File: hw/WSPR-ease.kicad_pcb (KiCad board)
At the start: 4 copper layers, 99 x 64 mm, 169 parts, among them IC401 SN74AHCT1G125DRLR, IC402 SN74AHCT1G125DRLR, IC403 SN74AHCT1G125DRLR, IC501 SN74AHCT1G125DRLR, IC502 SN74AHCT1G125DRLR, IC503 SN74AHCT1G125DRLR, IC601 SN74AHCT1G125DRLR, IC602 SN74AHCT1G125DRLR, IC603 SN74AHCT1G125DRLR, IC701 SN74AHCT1G125DRLR, IC702 SN74AHCT1G125DRLR, IC703 SN74AHCT1G125DRLR, J101 SMA, J102 pwr+data, J103 SMA, K201 G6K-2, K202 G6K-2, K203 G6K-2, Q101 2N7002H, Q201 2N7002H, Q202 2N7002H, Q203 2N7002H, Q401 MMBF170, Q402 MMBF170, Q403 MMBF170, Q501 MMBF170, Q502 MMBF170, Q503 MMBF170, Q601 MMBF170, Q602 MMBF170, Q603 MMBF170, Q701 MMBF170, Q702 MMBF170, Q703 MMBF170, T301 BN-43-202_DualPri_CTSec, U101 GNSS module, U102 ESP32-S3-WROOM-1-N8R8, U103 SRV05-4, U104 TPS74612PQWDRBRQ1, U105 TPS22918DBVR, U106 LMR51430YDDCR, U301 ICE40UP5K-SG48ITR, Y301 40MHz

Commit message: Timing now closes at 121MHz. But output still does not produce any signal on my scope. Shit.
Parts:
- removed C201, C211: 100nF X7R 50V, Capacitor_SMD:C_0603_1608Metric
- moved L205 0.06 mm to (115.6, 94.5)
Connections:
- K201 pad 4: Net-(C201-Pad2) -> /Low Pass Filters/RFin
- K201 pad 5: Net-(C211-Pad1) -> /Low Pass Filters/RFout
- K202 pad 4: Net-(C201-Pad2) -> /Low Pass Filters/RFin
- K202 pad 5: Net-(C211-Pad1) -> /Low Pass Filters/RFout
- K203 pad 4: Net-(C201-Pad2) -> /Low Pass Filters/RFin
- K203 pad 5: Net-(C211-Pad1) -> /Low Pass Filters/RFout
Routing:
- net /Low Pass Filters/RFout: track 7.32 -> 88.2 mm, vias 0 -> 4
- net Net-(C211-Pad1): track 79.6 -> 0.00 mm, vias 4 -> 0
- net /Low Pass Filters/RFin: track 17.3 -> 90.0 mm, vias 0 -> 4
- net Net-(C201-Pad2): track 71.7 -> 0.00 mm, vias 4 -> 0

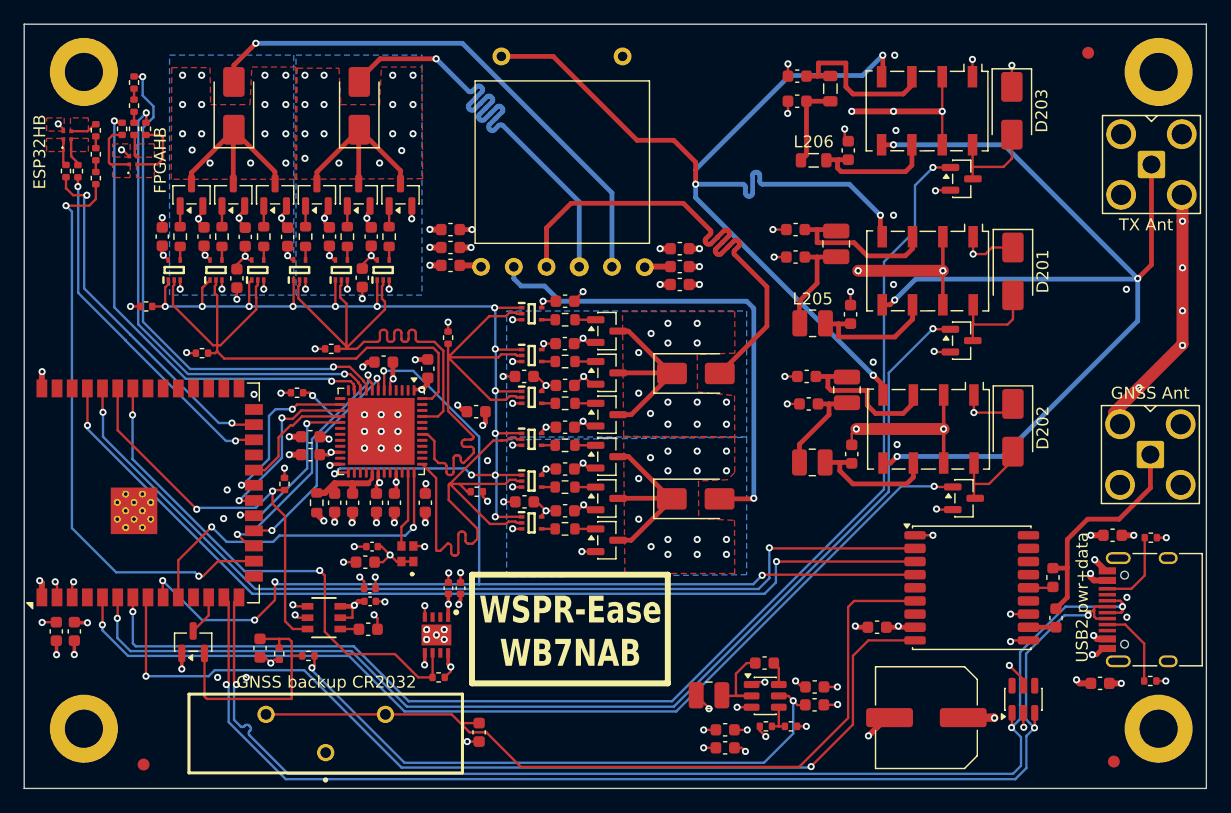
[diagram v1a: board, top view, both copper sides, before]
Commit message: Use VFPGAIO for pullup for driverNEN. Fix some layout issues with more equal routing lengths in critical tx phase paths.
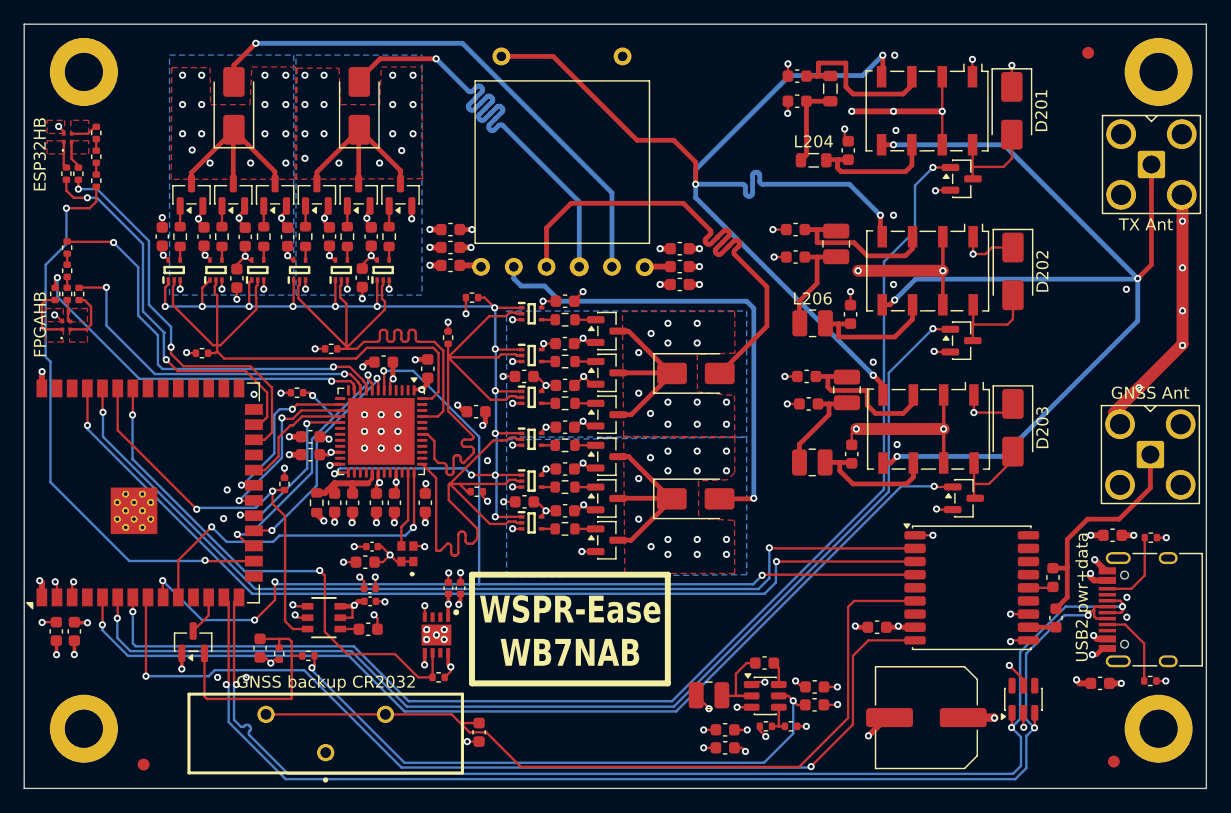
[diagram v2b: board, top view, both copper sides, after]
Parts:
- moved R306 27.3 mm to (87.1, 92.3)
- moved R301 14.9 mm to (53.2, 88.1)
- moved R302 14.9 mm to (53.2, 90.0)
- moved D301 14.9 mm to (53.1, 94.6)
- moved R303 14.9 mm to (54.2, 92.0)
- moved R304 14.9 mm to (52.2, 92.0)
- moved R305 14.9 mm to (53.2, 92.0)
- moved D101 0.22 mm to (53.2, 78.9)
- moved R107 0.22 mm to (54.1, 81.9)
- moved R103 0.22 mm to (55.6, 82.5)
- moved R106 0.22 mm to (55.6, 80.5)
- moved R108 0.22 mm to (53.1, 81.9)
- moved R109 0.22 mm to (55.6, 78.5)
- renumbered C204 to C201, C207 to C204, C210 to C207, C402 to C401, C401 to C402, C502 to C501, C501 to C502, C602 to C601, C601 to C602, C702 to C701, C701 to C702, D203 to D201, D201 to D202, D202 to D203, IC402 to IC401, IC401 to IC402, IC502 to IC501, IC501 to IC502, IC602 to IC601, IC601 to IC602, IC702 to IC701, IC701 to IC702, K203 to K201, K201 to K202, K202 to K203, L203 to L201, L201 to L202, L202 to L203, L206 to L204, L204 to L205, L205 to L206, Q203 to Q201, Q201 to Q203, R107 to R103, R108 to R104, R109 to R105, R110 to R106, R111 to R107, R112 to R108, R113 to R109, R114 to R110, R115 to R111, R116 to R112, R117 to R113
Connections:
- R306 pad 2: +3.3V -> +VFPGAIO
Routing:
- net /Transmitter/hbG: track 40.0 -> 29.3 mm
- net /Transmitter/hbR: track 43.5 -> 34.5 mm
- net /Transmitter/hbB: track 39.6 -> 30.9 mm
- net Net-(U102-IO47): track 29.6 -> 33.9 mm
- net Net-(U102-IO48): track 29.8 -> 32.3 mm
- net +VFPGAIO: track 18.3 -> 19.6 mm, vias 9 -> 10
- net /Transmitter/grn: track 5.65 -> 4.64 mm
- net Net-(U102-IO46): track 48.6 -> 47.6 mm
- net +3.3V: track 24.6 -> 23.8 mm, vias 18 -> 17
- net /Transmitter/driverNEN: track 88.1 -> 88.8 mm

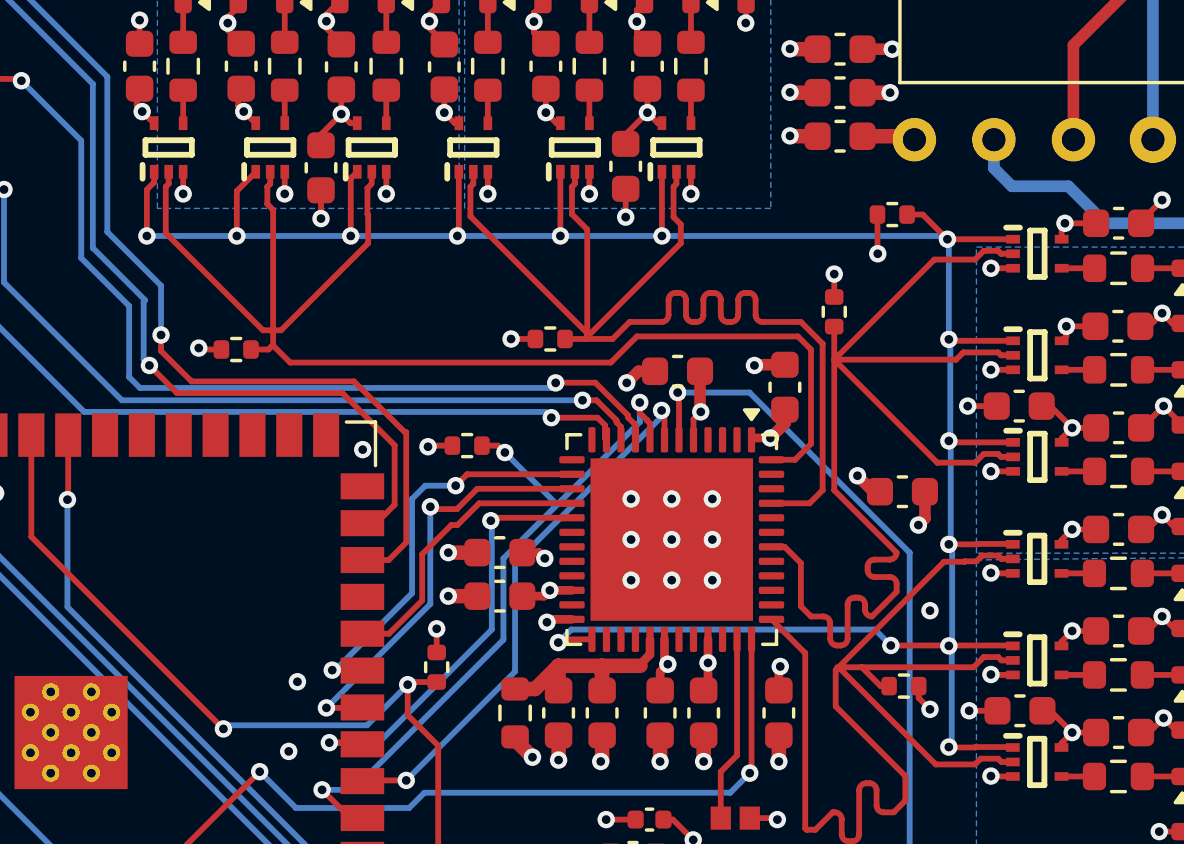
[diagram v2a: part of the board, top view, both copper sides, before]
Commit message: I think this is now using the SB_MAC16 properly for each instance. The AI based configs were all screwed up. I listed teh name from the iCE40 Tech Lib doc for each flavor used in a comment to help if changes are needed later. Also silkscreen labels for the four FPGA output pins for probing. I also fixed some stuff in the SB_IO sim cells_sim.v that seemed wrong but now it matches the PDF block diagram AFACT.
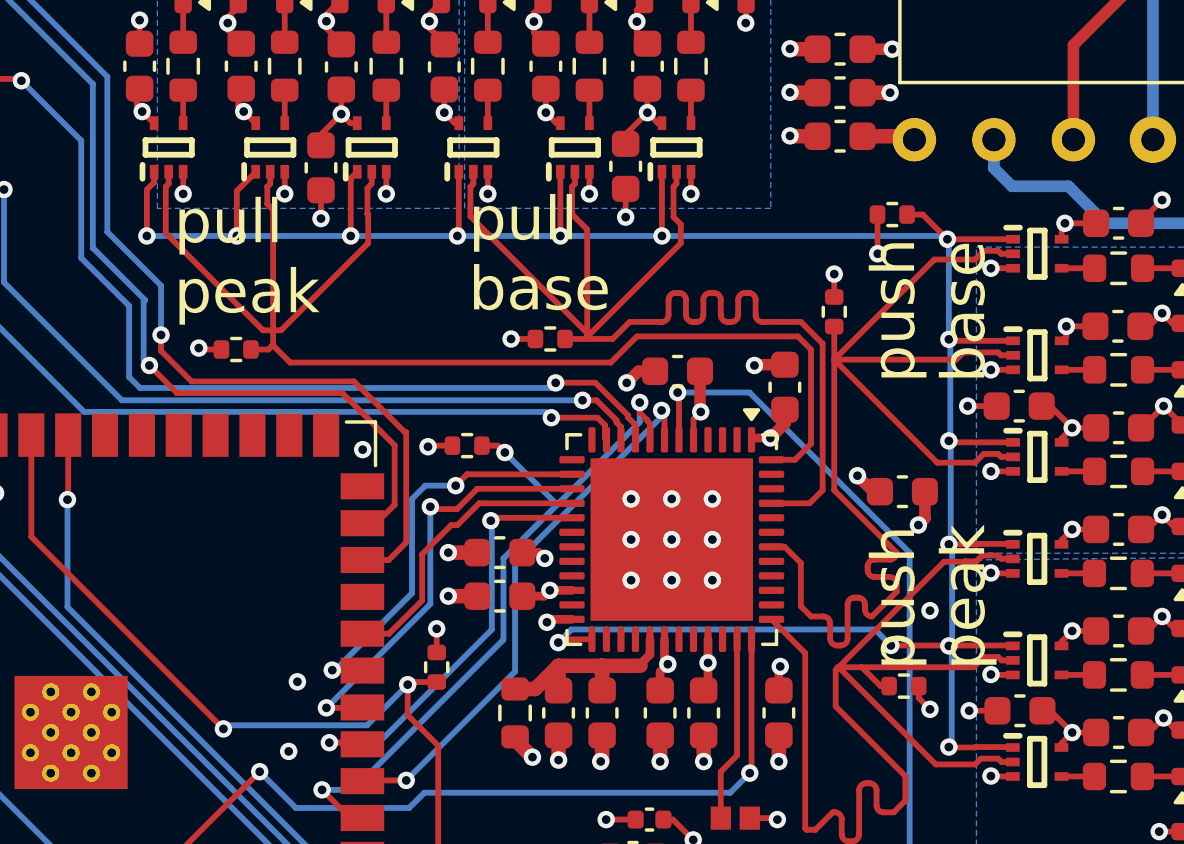
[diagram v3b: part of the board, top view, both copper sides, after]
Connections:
- net /Transmitter/pull1 renamed /Transmitter/pullBase
- net /Transmitter/pull1D renamed /Transmitter/pullBaseD
- net /Transmitter/pull1T renamed /Transmitter/pullBaseT
- net /Transmitter/pull2 renamed /Transmitter/pullPeak
- net /Transmitter/pull2D renamed /Transmitter/pullPeakD
- net /Transmitter/pull2T renamed /Transmitter/pullPeakT
- net /Transmitter/push1 renamed /Transmitter/pushBase
- net /Transmitter/push1D renamed /Transmitter/pushBaseD
- net /Transmitter/push1T renamed /Transmitter/pushBaseT
- net /Transmitter/push2 renamed /Transmitter/pushPeak
- net /Transmitter/push2D renamed /Transmitter/pushPeakD
- net /Transmitter/push2T renamed /Transmitter/pushPeakT
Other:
- board text added: "pull base"
- board text added: "pull peak"
- board text added: "push base"
- board text added: "push peak"

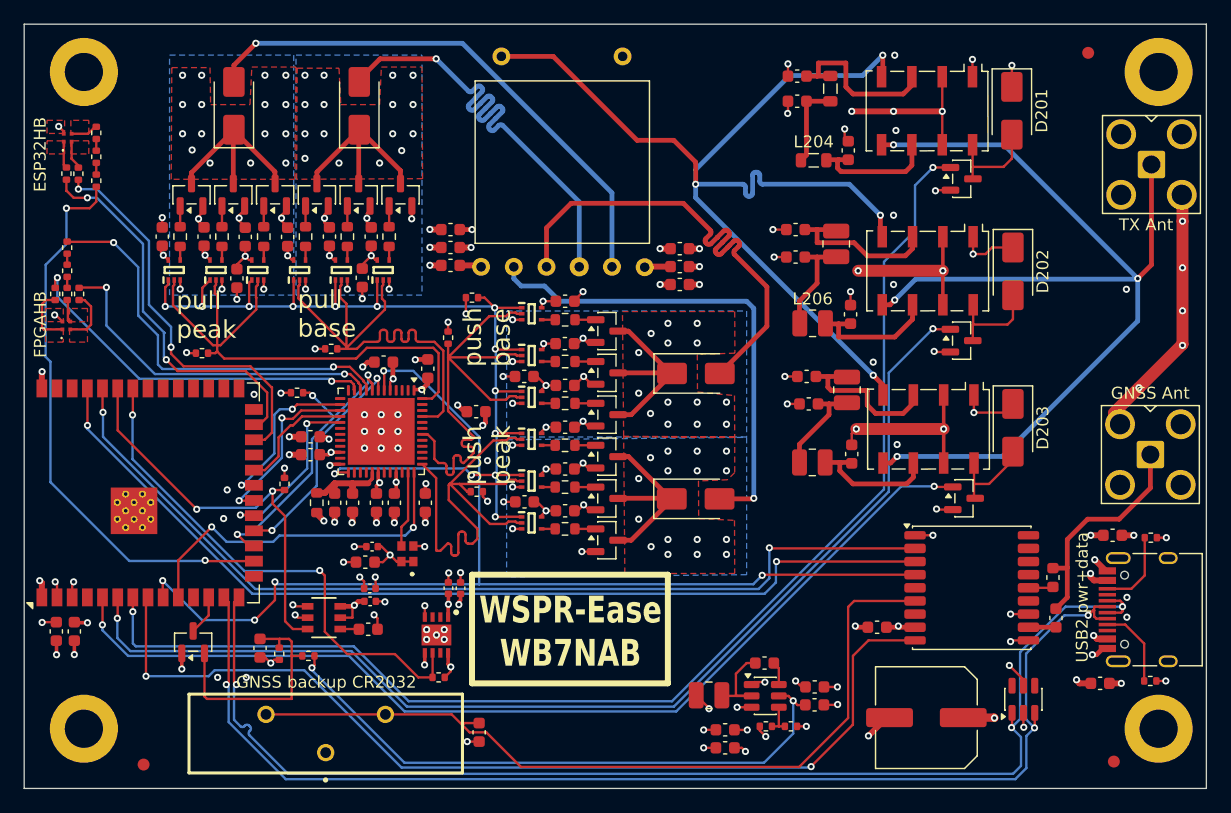
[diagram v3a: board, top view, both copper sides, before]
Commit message: Fucking USB 16-pin footprint! Also, completely redid the layout and wiring of the transmitter using a MOSFET gate and R+diode gate drive, simplify BOM, enhance LPFs for square wave output >= 10MHz.
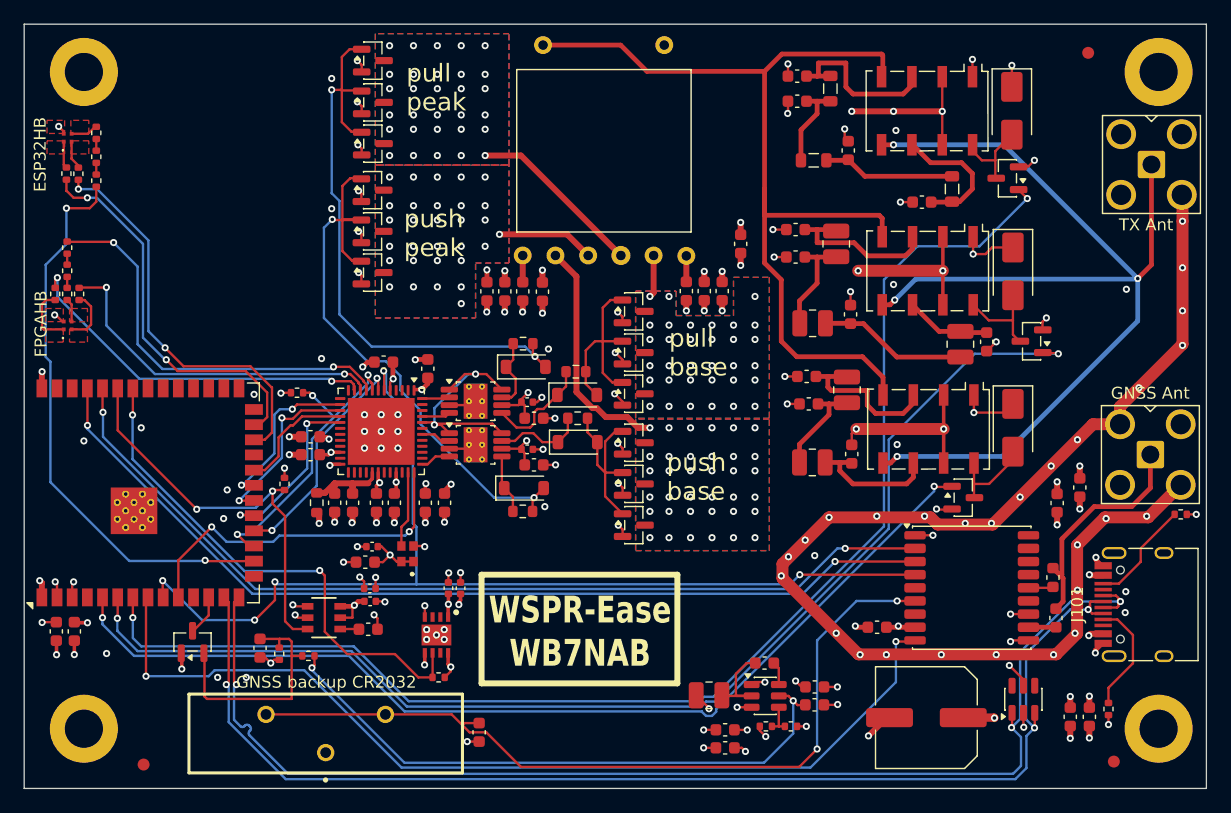
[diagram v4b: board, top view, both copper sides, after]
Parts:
- removed C403, C503, C601, C602, C603, C701, C702, C703: 100nF X7R 50V, Capacitor_SMD:C_0603_1608Metric
- removed D601, D701: SS14, Diode_SMD:D_SMA
- removed IC401, IC402, IC403, IC501, IC502, IC503, IC601, IC602, IC603, IC701, IC702, IC703: SN74AHCT1G125DRLR, Library:SOTFL50P160X60-5N
- removed Q601, Q602, Q603, Q701, Q702, Q703: MMBF170, Package_TO_SOT_SMD:SOT-23
- removed the R306 at (87.1, 92.3)
- removed R308, R309, R310, R311: 10k, Resistor_SMD:R_0402_1005Metric
- removed R403, R503, R601, R602, R603, R701, R702, R703: 10, Resistor_SMD:R_0603_1608Metric
- added C207: 150pF NP0 100V, Capacitor_SMD:C_0603_1608Metric, F.Cu at (130.2, 96.0)
- added C211: 82pF NP0 100V, Capacitor_SMD:C_0603_1608Metric, F.Cu at (124.8, 84.3)
- added D402: 1N4148W, Diode_SMD:D_SOD-123, F.Cu at (91.5, 108.2)
- added D502: 1N4148W, Diode_SMD:D_SOD-123, F.Cu at (95.9, 100.5)
- added L205: 560nH, Inductor_SMD:L_1008_2520Metric, F.Cu at (128.0, 96.2)
- added L208: 270nH, Inductor_SMD:L_0805_2012Metric, F.Cu at (127.3, 83.2)
- added Q404: MMBF170, Package_TO_SOT_SMD:SOT-23, F.Cu at (78.8, 83.3)
- added Q405: MMBF170, Package_TO_SOT_SMD:SOT-23, F.Cu at (78.8, 86.8)
- added Q406: MMBF170, Package_TO_SOT_SMD:SOT-23, F.Cu at (78.8, 90.2)
- added Q504: MMBF170, Package_TO_SOT_SMD:SOT-23, F.Cu at (100.6, 93.5)
- added Q505: MMBF170, Package_TO_SOT_SMD:SOT-23, F.Cu at (100.6, 96.9)
- added Q506: MMBF170, Package_TO_SOT_SMD:SOT-23, F.Cu at (100.6, 100.3)
- added U401: UCC27524DGN, Package_SO:Texas_DGN0008G_VSSOP-8-1EP_3x3mm_P0.65mm_EP2x2.94mm_Mask1.846x2.15mm_ThermalVias, F.Cu at (87.4, 104.6)
- added U501: UCC27524DGN, Package_SO:Texas_DGN0008G_VSSOP-8-1EP_3x3mm_P0.65mm_EP2x2.94mm_Mask1.846x2.15mm_ThermalVias, F.Cu at (87.4, 101.0)
- C204: renamed from C203; value 220pF NP0 100V -> 150pF NP0 100V
- C205: renamed from C206; value 470pF NP0 100V -> 330pF NP0 100V
- C206: renamed from C209; value 220pF NP0 100V -> 330pF NP0 100V
- C208: renamed from C201; value 100pF NP0 100V -> 82pF NP0 100V
- C209: renamed from C204; value 220pF NP0 100V -> 180pF NP0 100V
- C210: renamed from C207; value 100pF NP0 100V -> 180pF NP0 100V
- C401, C501: value 100nF X7R 50V -> 1uF; footprint Capacitor_SMD:C_0603_1608Metric -> Capacitor_SMD:C_0402_1005Metric
- D401, D501: value SS14 -> 1N4148W; footprint Diode_SMD:D_SMA -> Diode_SMD:D_SOD-123
- L204: renamed from L206; value 560nH -> 680nH
- L207: renamed from L204; value 270nH -> 330nH
- Q101, Q201, Q202, Q203: value 2N7002H -> MMBF170
- moved C307 49.1 mm to (137.2, 127.4), turned to 90 degrees
- moved C306 47.4 mm to (138.0, 108.2), turned to -90 degrees
- moved Q503 38.6 mm to (78.8, 79.4)
- moved Q501 38.5 mm to (78.8, 72.5)
- moved Q502 38.5 mm to (78.8, 76.0)
- moved C305 31.8 mm to (109.6, 87.8), turned to -90 degrees
- moved Q203 27.0 mm to (131.9, 82.3), turned to 180 degrees
- moved Q201 26.7 mm to (128.2, 109.0)
- moved C301 25.6 mm to (93.0, 91.8)
- moved D501 18.0 mm to (91.6, 98.1)
- moved R402 13.0 mm to (91.3, 110.2)
- moved C401 12.8 mm to (91.7, 105.0)
- moved D401 11.4 mm to (96.0, 104.4)
- moved C402 10.5 mm to (92.3, 106.3)
- moved R502 9.71 mm to (95.8, 98.5)
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- renumbered C110 to C101, C111 to C102, C105 to C103, C112 to C104, C106 to C105, C101 to C106, C103 to C107, C104 to C108, C102 to C109, C115 to C110, C113 to C111, C114 to C112, C116 to C113, C117 to C114, C108 to C115, C109 to C116, C107 to C117, C202 to C201, C205 to C202, C208 to C203, C309 to C301, C316 to C302, C318 to C303, C321 to C304, C307 to C305, C310 to C306, C308 to C307, C301 to C308, C302 to C309, C313 to C310, C317 to C311, C319 to C312, C320 to C313, C324 to C314, C314 to C315, C311 to C316, C315 to C317, C312 to C318, C322 to C319, C303 to C320, C305 to C321, C323 to C322, C304 to C323, C306 to C324, D203 to D201, D201 to D203, J102 to J101, J103 to J102, J101 to J103, K202 to K201, K203 to K202, K201 to K203, L202 to L201, L205 to L202, L201 to L206, R110 to R101, R111 to R102, R101 to R103, R102 to R104, R103 to R105, R109 to R107, R107 to R108, R108 to R109, R104 to R110, R112 to R111, R113 to R112, R105 to R113, R305 to R303, R303 to R304, R304 to R305, R307 to R306, R312 to R307, U103 to U101, U106 to U103, U101 to U104, U104 to U105, U105 to U106
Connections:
- C206 pad 1: Net-(C209-Pad1) (its old number) -> Net-(C206-Pad1)
- C210 pad 1: Net-(C207-Pad1) -> Net-(C210-Pad1)
- D201 pad 2: Net-(D203-A) -> Net-(D201-A)
- D203 pad 2: Net-(D201-A) -> Net-(D203-A)
- D401 pad 1: /Transmitter/pushBaseD -> Net-(D401-K)
- D401 pad 2: /Transmitter/pushBaseT -> Net-(D401-A)
- D501 pad 1: /Transmitter/pushPeakD -> Net-(D501-K)
- D501 pad 2: /Transmitter/pushPeakT -> Net-(D501-A)
- K201 pad 8: Net-(D203-A) -> Net-(D201-A)
- K202 pad 6: Net-(C209-Pad1) (its old number) -> Net-(C207-Pad1)
- K203 pad 6: Net-(C207-Pad1) -> Net-(C211-Pad1)
- K203 pad 8: Net-(D201-A) -> Net-(D203-A)
- L204 pad 2: Net-(C209-Pad1) (its old number) -> Net-(C206-Pad1)
- L207 pad 2: Net-(C207-Pad1) -> Net-(C210-Pad1)
- Q201 pad 1: /hiON -> /loON
- Q203 pad 1: /loON -> /hiON
- Q401 pad 1: Net-(Q401-G) -> Net-(D401-A)
- Q401 pad 3: /Transmitter/pushBaseD -> /Transmitter/pushBaseT
- Q402 pad 1: Net-(Q402-G) -> Net-(D401-A)
- Q402 pad 3: /Transmitter/pushBaseD -> /Transmitter/pushBaseT
- Q403 pad 1: Net-(Q403-G) -> Net-(D401-A)
- Q403 pad 3: /Transmitter/pushBaseD -> /Transmitter/pushBaseT
- Q501 pad 1: Net-(Q501-G) -> Net-(D501-A)
- Q501 pad 3: /Transmitter/pushPeakD -> /Transmitter/pullPeakT
- Q502 pad 1: Net-(Q502-G) -> Net-(D501-A)
- Q502 pad 3: /Transmitter/pushPeakD -> /Transmitter/pullPeakT
- Q503 pad 1: Net-(Q503-G) -> Net-(D501-A)
- Q503 pad 3: /Transmitter/pushPeakD -> /Transmitter/pullPeakT
- R401 pad 1: Net-(IC401-Y) -> Net-(D401-K)
- R401 pad 2: Net-(Q401-G) -> Net-(D401-A)
- R402 pad 2: Net-(Q402-G) -> Net-(D402-A)
- R501 pad 1: Net-(IC501-Y) -> Net-(D501-K)
- R501 pad 2: Net-(Q501-G) -> Net-(D501-A)
- R502 pad 2: Net-(Q502-G) -> Net-(D502-A)
- T301 pad 2: /Transmitter/pullPeakT -> /Transmitter/pullBaseT
- T301 pad 3: /Transmitter/pullBaseT -> /Transmitter/pullPeakT
- T301 pad 4: /Transmitter/pushBaseT -> /Transmitter/pushPeakT
- T301 pad 5: /Transmitter/pushPeakT -> /Transmitter/pushBaseT
- U301 pad 25: /Transmitter/driverNEN -> unconnected-(U301A-IOT_36b-Pad25)
- U301 pad 44: unconnected-(U301C-IOB_3b_G6-Pad44) -> /Transmitter/driverEN
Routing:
- net /Transmitter/driverNEN: track 88.8 -> 0.00 mm, vias 14 -> 0
- net GND: track 167.8 -> 237.2 mm, vias 138 -> 153
- net Net-(D501-A): track 0.00 -> 51.2 mm, vias 0 -> 2
- net Net-(D402-A): track 0.00 -> 49.5 mm, vias 0 -> 2
- net /Transmitter/pullPeak: track 45.4 -> 2.16 mm
- net /Transmitter/pushPeak: track 43.2 -> 2.53 mm
- net /Transmitter/pushBase: track 42.6 -> 2.49 mm
- net /Transmitter/pullBase: track 41.6 -> 2.39 mm
- net /Transmitter/pullBaseT: track 40.0 -> 3.56 mm, vias 1 -> 33
- net /Transmitter/pushPeakT: track 40.9 -> 8.16 mm, vias 1 -> 30
- net /Transmitter/pullPeakT: track 45.2 -> 14.8 mm, vias 1 -> 30
- net /Transmitter/pushBaseT: track 41.2 -> 19.6 mm, vias 0 -> 36
- net /Transmitter/driverEN: track 0.00 -> 20.2 mm, vias 0 -> 2
- net Net-(D502-A): track 0.00 -> 16.9 mm
- net /Transmitter/pullPeakD: track 16.4 -> 0.00 mm, vias 16 -> 0
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- added copper zone on B.Cu, net /Transmitter/pullBaseT
- added copper zone on F.Cu, net /Transmitter/pullBaseT
- added copper zone on B.Cu, net /Transmitter/pullPeakT
- added copper zone on F.Cu, net /Transmitter/pullPeakT
- added copper zone on B.Cu, net /Transmitter/pushBaseT
- added copper zone on F.Cu, net /Transmitter/pushBaseT
- added copper zone on B.Cu, net /Transmitter/pushPeakT
- added copper zone on F.Cu, net /Transmitter/pushPeakT
- removed copper zone on B.Cu, net /Transmitter/pullBaseD
- removed copper zone on F.Cu, net /Transmitter/pullBaseD
- removed copper zone on B.Cu, net /Transmitter/pullPeakD
- removed copper zone on F.Cu, net /Transmitter/pullPeakD
- removed copper zone on B.Cu, net /Transmitter/pushBaseD
- removed copper zone on F.Cu, net /Transmitter/pushBaseD
- removed copper zone on B.Cu, net /Transmitter/pushPeakD
- removed copper zone on F.Cu, net /Transmitter/pushPeakD
